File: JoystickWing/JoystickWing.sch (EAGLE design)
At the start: 19 parts, among them J1 5747844-4

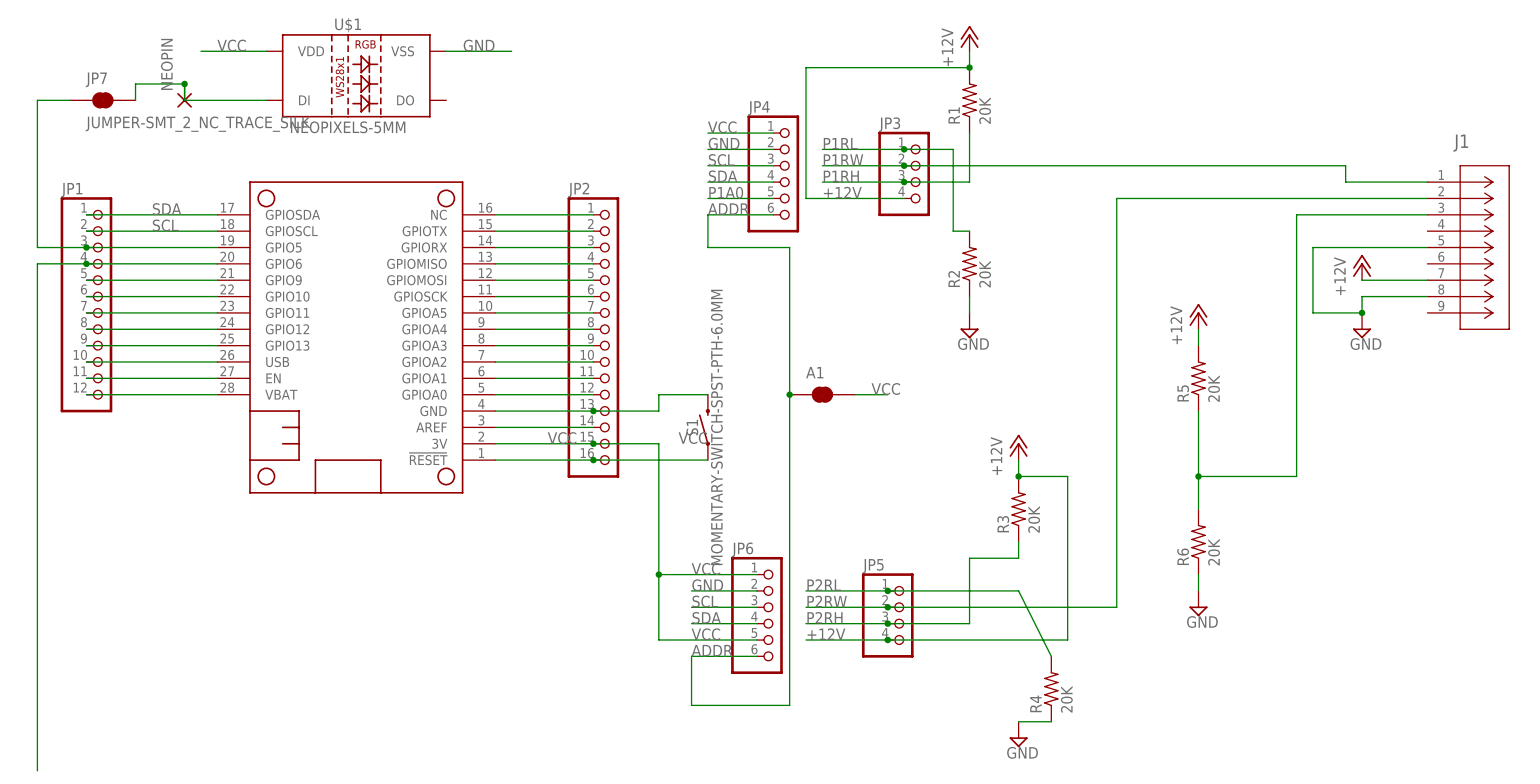
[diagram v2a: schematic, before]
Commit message: Added the missing Neopixel led pads and updated the switch to DTS-3: 3.5x6mm style switch.
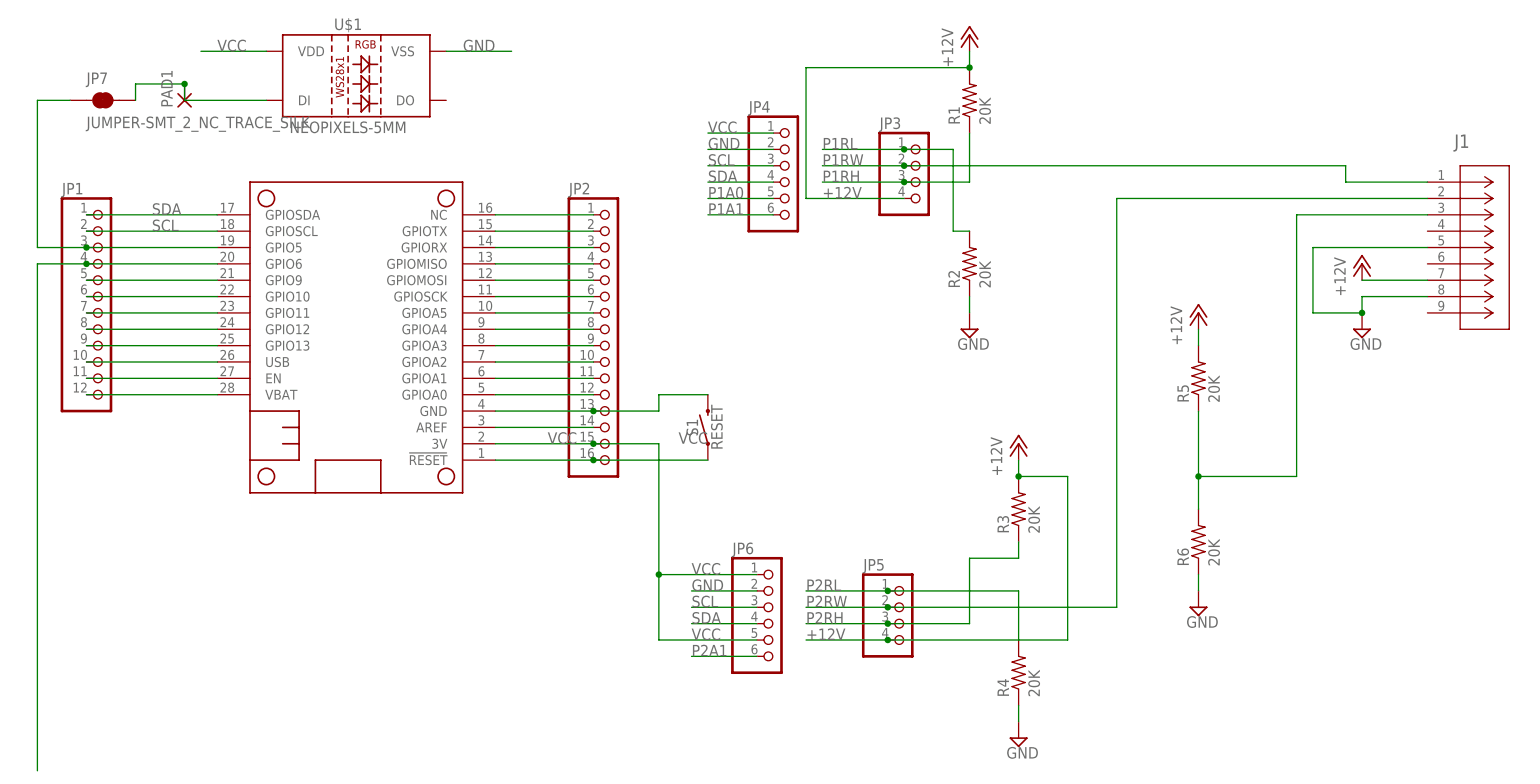
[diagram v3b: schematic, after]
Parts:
- removed A1: JUMPER-SMT_2_NC_TRACE_SILK, SparkFun-Jumpers:JUMPER-SMT_2_NC_TRACE_SILK
- S1: value MOMENTARY-SWITCH-SPST-PTH-6.0MM -> RESET; device SparkFun-Switches:MOMENTARY-SWITCH-SPST-PTH-6.0MM -> milador:SWITCH_DTS-3
- renumbered NEOPIN to PAD1
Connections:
- removed net ADDR: A1.1, JP4.6, JP6.6
- new net P1A1: JP4.6
- new net P2A1: JP6.6
- net VCC: no longer A1.2
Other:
- moved on the sheet: R4
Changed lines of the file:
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@@
 <?xml version="1.0" encoding="utf-8"?>
 <!DOCTYPE eagle SYSTEM "eagle.dtd">
-<eagle version="9.2.2">
+<eagle version="9.4.2">
 <drawing>
 <settings>
@@
 <layers>
 <layer number="1" name="Top" color="4" fill="1" visible="no" active="no"/>
+<layer number="2" name="Route2" color="1" fill="3" visible="no" active="no"/>
+<layer number="3" name="Route3" color="4" fill="3" visible="no" active="no"/>
+<layer number="4" name="Route4" color="1" fill="4" visible="no" active="no"/>
+<layer number="5" name="Route5" color="4" fill="4" visible="no" active="no"/>
+<layer number="6" name="Route6" color="1" fill="8" visible="no" active="no"/>
+<layer number="7" name="Route7" color="4" fill="8" visible="no" active="no"/>
+<layer number="8" name="Route8" color="1" fill="2" visible="no" active="no"/>
+<layer number="9" name="Route9" color="4" fill="2" visible="no" active="no"/>
+<layer number="10" name="Route10" color="1" fill="7" visible="no" active="no"/>
+<layer number="11" name="Route11" color="4" fill="7" visible="no" active="no"/>
+<layer number="12" name="Route12" color="1" fill="5" visible="no" active="no"/>
+<layer number="13" name="Route13" color="4" fill="5" visible="no" active="no"/>
+<layer number="14" name="Route14" color="1" fill="6" visible="no" active="no"/>
+<layer number="15" name="Route15" color="4" fill="6" visible="no" active="no"/>
 <layer number="16" name="Bottom" color="1" fill="1" visible="no" active="no"/>
 <layer number="17" name="Pads" color="2" fill="1" visible="no" active="no"/>
@@
 <part name="JP1" library="adafruit" library_urn="urn:adsk.eagle:library:420" deviceset="PINHD-1X12" device="-CB" package3d_urn="urn:adsk.eagle:package:6240772/1"/>
 <part name="JP2" library="pinhead" library_urn="urn:adsk.eagle:library:325" deviceset="PINHD-1X16" device="" package3d_urn="urn:adsk.eagle:package:22432/2"/>
-<part name="U$1" library="milador" deviceset="NEOPIXELS-5MM" device="" package3d_urn="urn:adsk.eagle:package:6677832/4"/>
+<part name="U$1" library="milador" library_urn="urn:adsk.eagle:library:12595918" deviceset="NEOPIXELS-5MM" device="" package3d_urn="urn:adsk.eagle:package:6677832/5"/>
 <part name="JP7" library="SparkFun-Jumpers" deviceset="JUMPER-SMT_2_NC_TRACE" device="_SILK"/>
-<part name="NEOPIN" library="wirepad" library_urn="urn:adsk.eagle:library:412" deviceset="2,54/1,1" device="" package3d_urn="urn:adsk.eagle:package:30836/1"/>
-<part name="S1" library="SparkFun-Switches" library_urn="urn:adsk.eagle:library:535" deviceset="MOMENTARY-SWITCH-SPST" device="-PTH-6.0MM" package3d_urn="urn:adsk.eagle:package:40163/1"/>
-<part name="A1" library="SparkFun-Jumpers" deviceset="JUMPER-SMT_2_NC_TRACE" device="_SILK"/>
+<part name="PAD1" library="wirepad" library_urn="urn:adsk.eagle:library:412" deviceset="2,54/1,1" device="" package3d_urn="urn:adsk.eagle:package:30836/1"/>
+<part name="S1" library="milador" library_urn="urn:adsk.eagle:library:12595918" deviceset="SWITCH_DTS-3" device="" value="RESET"/>
 </parts>
 <sheets>
@@
 <attribute name="VALUE" x="28.702" y="19.05" size="1.778" layer="96" rot="R90"/>
 </instance>
-<instance part="R4" gate="G$1" x="30.48" y="-5.08" smashed="yes" rot="R90">
-<attribute name="NAME" x="28.9814" y="-8.89" size="1.778" layer="95" rot="R90"/>
-<attribute name="VALUE" x="33.782" y="-8.89" size="1.778" layer="96" rot="R90"/>
+<instance part="R4" gate="G$1" x="25.4" y="-2.54" smashed="yes" rot="R90">
+<attribute name="NAME" x="23.9014" y="-6.35" size="1.778" layer="95" rot="R90"/>
+<attribute name="VALUE" x="28.702" y="-6.35" size="1.778" layer="96" rot="R90"/>
 </instance>
 <instance part="SUPPLY4" gate="GND" x="53.34" y="7.62" smashed="yes">
@@
 <attribute name="VALUE" x="-119.38" y="83.82" size="1.778" layer="96" font="vector" align="top-left"/>
 </instance>
-<instance part="NEOPIN" gate="1" x="-104.14" y="86.36" smashed="yes" rot="R90">
-<attribute name="NAME" x="-105.9942" y="87.757" size="1.778" layer="95" rot="R90"/>
+<instance part="PAD1" gate="1" x="-104.14" y="86.36" smashed="yes" rot="R90">
+<attribute name="NAME" x="-105.9942" y="85.217" size="1.778" layer="95" rot="R90"/>
 <attribute name="VALUE" x="-100.838" y="85.217" size="1.778" layer="96" rot="R90"/>
 </instance>
@@
 <attribute name="NAME" x="-24.384" y="35.56" size="1.778" layer="95" font="vector" rot="R90" align="bottom-center"/>
 <attribute name="VALUE" x="-22.352" y="35.56" size="1.778" layer="96" font="vector" rot="R90" align="top-center"/>
-</instance>
-<instance part="A1" gate="G$1" x="-5.08" y="40.64" smashed="yes">
-<attribute name="NAME" x="-7.62" y="43.18" size="1.778" layer="95" font="vector"/>
 </instance>
 </instances>
@@
 <pinref part="R4" gate="G$1" pin="1"/>
 <pinref part="SUPPLY3" gate="GND" pin="GND"/>
-<wire x1="30.48" y1="-10.16" x2="25.4" y2="-10.16" width="0.1524" layer="91"/>
+<wire x1="25.4" y1="-7.62" x2="25.4" y2="-10.16" width="0.1524" layer="91"/>
 </segment>
 <segment>
@@
 <label x="-99.06" y="93.98" size="1.778" layer="95"/>
 </segment>
-<segment>
-<pinref part="A1" gate="G$1" pin="2"/>
-<wire x1="0" y1="40.64" x2="5.08" y2="40.64" width="0.1524" layer="91"/>
-<label x="2.54" y="40.64" size="1.778" layer="95"/>
-</segment>
 </net>
 <net name="P1A0" class="0">
@@
 <wire x1="-12.7" y1="71.12" x2="-22.86" y2="71.12" width="0.1524" layer="91"/>
 <label x="-22.86" y="71.12" size="1.778" layer="95"/>
+</segment>
+</net>
+<net name="P1A1" class="0">
+<segment>
+<pinref part="JP4" gate="A" pin="6"/>
+<wire x1="-12.7" y1="68.58" x2="-22.86" y2="68.58" width="0.1524" layer="91"/>
+<label x="-22.86" y="68.58" size="1.778" layer="95"/>
 </segment>
 </net>
@@
 </segment>
 </net>
-<net name="ADDR" class="0">
+<net name="P2A1" class="0">
 <segment>
 <pinref part="JP6" gate="A" pin="6"/>
 <wire x1="-15.24" y1="0" x2="-25.4" y2="0" width="0.1524" layer="91"/>
 <label x="-25.4" y="0" size="1.778" layer="95"/>
-<wire x1="-25.4" y1="0" x2="-25.4" y2="-7.62" width="0.1524" layer="91"/>
-<wire x1="-25.4" y1="-7.62" x2="-10.16" y2="-7.62" width="0.1524" layer="91"/>
-<pinref part="A1" gate="G$1" pin="1"/>
-<wire x1="-10.16" y1="-7.62" x2="-10.16" y2="40.64" width="0.1524" layer="91"/>
-<wire x1="-10.16" y1="40.64" x2="-10.16" y2="63.5" width="0.1524" layer="91"/>
-<junction x="-10.16" y="40.64"/>
-<wire x1="-10.16" y1="63.5" x2="-22.86" y2="63.5" width="0.1524" layer="91"/>
-<pinref part="JP4" gate="A" pin="6"/>
-<wire x1="-12.7" y1="68.58" x2="-22.86" y2="68.58" width="0.1524" layer="91"/>
-<label x="-22.86" y="68.58" size="1.778" layer="95"/>
-<wire x1="-22.86" y1="63.5" x2="-22.86" y2="68.58" width="0.1524" layer="91"/>
 </segment>
 </net>
@@
 <pinref part="R4" gate="G$1" pin="2"/>
 <wire x1="5.08" y1="10.16" x2="25.4" y2="10.16" width="0.1524" layer="91"/>
-<wire x1="25.4" y1="10.16" x2="30.48" y2="0" width="0.1524" layer="91"/>
+<wire x1="25.4" y1="10.16" x2="25.4" y2="2.54" width="0.1524" layer="91"/>
 </segment>
 </net>
@@
 <segment>
 <pinref part="U$1" gate="G$1" pin="DI"/>
-<pinref part="NEOPIN" gate="1" pin="P"/>
+<pinref part="PAD1" gate="1" pin="P"/>
 <wire x1="-91.44" y1="86.36" x2="-104.14" y2="86.36" width="0.1524" layer="91"/>
 <wire x1="-104.14" y1="86.36" x2="-104.14" y2="88.9" width="0.1524" layer="91"/>

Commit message: Revert "Added the missing Neopixel led pads and updated the switch to DTS-3: 3.5x6mm style switch."
This reverts commit 7139ee0b9ca13871835c94f32c5504dad1631a27.
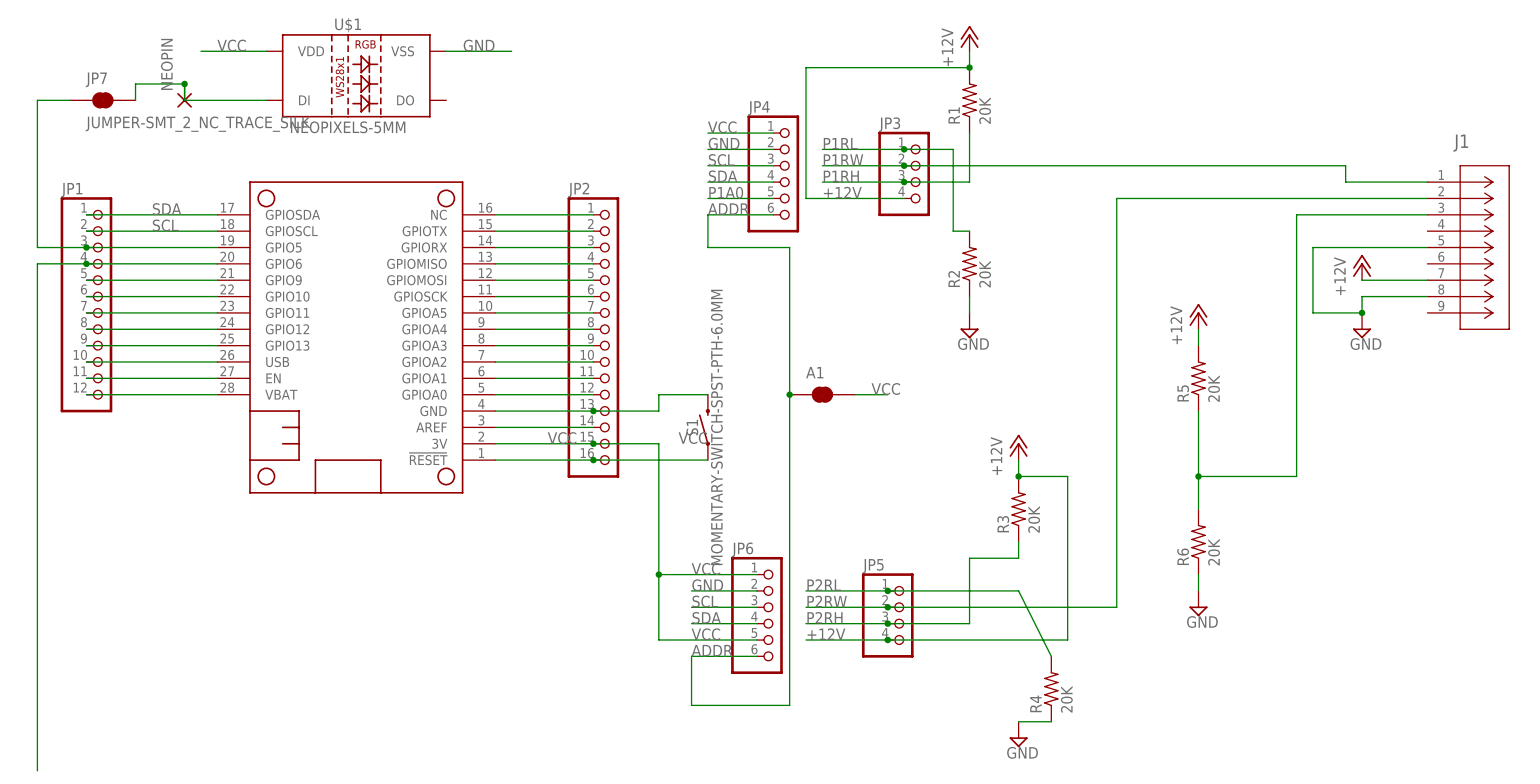
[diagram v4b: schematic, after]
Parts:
- added A1: JUMPER-SMT_2_NC_TRACE_SILK, SparkFun-Jumpers:JUMPER-SMT_2_NC_TRACE_SILK
- S1: value RESET -> MOMENTARY-SWITCH-SPST-PTH-6.0MM; device milador:SWITCH_DTS-3 -> SparkFun-Switches:MOMENTARY-SWITCH-SPST-PTH-6.0MM
- renumbered PAD1 to NEOPIN
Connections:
- removed net P1A1: JP4.6
- removed net P2A1: JP6.6
- new net ADDR: A1.1, JP4.6, JP6.6
- net VCC: now also A1.2
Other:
- moved on the sheet: R4
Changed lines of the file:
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@@
 <?xml version="1.0" encoding="utf-8"?>
 <!DOCTYPE eagle SYSTEM "eagle.dtd">
-<eagle version="9.4.2">
+<eagle version="9.2.2">
 <drawing>
 <settings>
@@
 <layers>
 <layer number="1" name="Top" color="4" fill="1" visible="no" active="no"/>
-<layer number="2" name="Route2" color="1" fill="3" visible="no" active="no"/>
-<layer number="3" name="Route3" color="4" fill="3" visible="no" active="no"/>
-<layer number="4" name="Route4" color="1" fill="4" visible="no" active="no"/>
-<layer number="5" name="Route5" color="4" fill="4" visible="no" active="no"/>
-<layer number="6" name="Route6" color="1" fill="8" visible="no" active="no"/>
-<layer number="7" name="Route7" color="4" fill="8" visible="no" active="no"/>
-<layer number="8" name="Route8" color="1" fill="2" visible="no" active="no"/>
-<layer number="9" name="Route9" color="4" fill="2" visible="no" active="no"/>
-<layer number="10" name="Route10" color="1" fill="7" visible="no" active="no"/>
-<layer number="11" name="Route11" color="4" fill="7" visible="no" active="no"/>
-<layer number="12" name="Route12" color="1" fill="5" visible="no" active="no"/>
-<layer number="13" name="Route13" color="4" fill="5" visible="no" active="no"/>
-<layer number="14" name="Route14" color="1" fill="6" visible="no" active="no"/>
-<layer number="15" name="Route15" color="4" fill="6" visible="no" active="no"/>
 <layer number="16" name="Bottom" color="1" fill="1" visible="no" active="no"/>
 <layer number="17" name="Pads" color="2" fill="1" visible="no" active="no"/>
@@
 <part name="JP1" library="adafruit" library_urn="urn:adsk.eagle:library:420" deviceset="PINHD-1X12" device="-CB" package3d_urn="urn:adsk.eagle:package:6240772/1"/>
 <part name="JP2" library="pinhead" library_urn="urn:adsk.eagle:library:325" deviceset="PINHD-1X16" device="" package3d_urn="urn:adsk.eagle:package:22432/2"/>
-<part name="U$1" library="milador" library_urn="urn:adsk.eagle:library:12595918" deviceset="NEOPIXELS-5MM" device="" package3d_urn="urn:adsk.eagle:package:6677832/5"/>
+<part name="U$1" library="milador" deviceset="NEOPIXELS-5MM" device="" package3d_urn="urn:adsk.eagle:package:6677832/4"/>
 <part name="JP7" library="SparkFun-Jumpers" deviceset="JUMPER-SMT_2_NC_TRACE" device="_SILK"/>
-<part name="PAD1" library="wirepad" library_urn="urn:adsk.eagle:library:412" deviceset="2,54/1,1" device="" package3d_urn="urn:adsk.eagle:package:30836/1"/>
-<part name="S1" library="milador" library_urn="urn:adsk.eagle:library:12595918" deviceset="SWITCH_DTS-3" device="" value="RESET"/>
+<part name="NEOPIN" library="wirepad" library_urn="urn:adsk.eagle:library:412" deviceset="2,54/1,1" device="" package3d_urn="urn:adsk.eagle:package:30836/1"/>
+<part name="S1" library="SparkFun-Switches" library_urn="urn:adsk.eagle:library:535" deviceset="MOMENTARY-SWITCH-SPST" device="-PTH-6.0MM" package3d_urn="urn:adsk.eagle:package:40163/1"/>
+<part name="A1" library="SparkFun-Jumpers" deviceset="JUMPER-SMT_2_NC_TRACE" device="_SILK"/>
 </parts>
 <sheets>
@@
 <attribute name="VALUE" x="28.702" y="19.05" size="1.778" layer="96" rot="R90"/>
 </instance>
-<instance part="R4" gate="G$1" x="25.4" y="-2.54" smashed="yes" rot="R90">
-<attribute name="NAME" x="23.9014" y="-6.35" size="1.778" layer="95" rot="R90"/>
-<attribute name="VALUE" x="28.702" y="-6.35" size="1.778" layer="96" rot="R90"/>
+<instance part="R4" gate="G$1" x="30.48" y="-5.08" smashed="yes" rot="R90">
+<attribute name="NAME" x="28.9814" y="-8.89" size="1.778" layer="95" rot="R90"/>
+<attribute name="VALUE" x="33.782" y="-8.89" size="1.778" layer="96" rot="R90"/>
 </instance>
 <instance part="SUPPLY4" gate="GND" x="53.34" y="7.62" smashed="yes">
@@
 <attribute name="VALUE" x="-119.38" y="83.82" size="1.778" layer="96" font="vector" align="top-left"/>
 </instance>
-<instance part="PAD1" gate="1" x="-104.14" y="86.36" smashed="yes" rot="R90">
-<attribute name="NAME" x="-105.9942" y="85.217" size="1.778" layer="95" rot="R90"/>
+<instance part="NEOPIN" gate="1" x="-104.14" y="86.36" smashed="yes" rot="R90">
+<attribute name="NAME" x="-105.9942" y="87.757" size="1.778" layer="95" rot="R90"/>
 <attribute name="VALUE" x="-100.838" y="85.217" size="1.778" layer="96" rot="R90"/>
 </instance>
@@
 <attribute name="NAME" x="-24.384" y="35.56" size="1.778" layer="95" font="vector" rot="R90" align="bottom-center"/>
 <attribute name="VALUE" x="-22.352" y="35.56" size="1.778" layer="96" font="vector" rot="R90" align="top-center"/>
+</instance>
+<instance part="A1" gate="G$1" x="-5.08" y="40.64" smashed="yes">
+<attribute name="NAME" x="-7.62" y="43.18" size="1.778" layer="95" font="vector"/>
 </instance>
 </instances>
@@
 <pinref part="R4" gate="G$1" pin="1"/>
 <pinref part="SUPPLY3" gate="GND" pin="GND"/>
-<wire x1="25.4" y1="-7.62" x2="25.4" y2="-10.16" width="0.1524" layer="91"/>
+<wire x1="30.48" y1="-10.16" x2="25.4" y2="-10.16" width="0.1524" layer="91"/>
 </segment>
 <segment>
@@
 <label x="-99.06" y="93.98" size="1.778" layer="95"/>
 </segment>
+<segment>
+<pinref part="A1" gate="G$1" pin="2"/>
+<wire x1="0" y1="40.64" x2="5.08" y2="40.64" width="0.1524" layer="91"/>
+<label x="2.54" y="40.64" size="1.778" layer="95"/>
+</segment>
 </net>
 <net name="P1A0" class="0">
@@
 <wire x1="-12.7" y1="71.12" x2="-22.86" y2="71.12" width="0.1524" layer="91"/>
 <label x="-22.86" y="71.12" size="1.778" layer="95"/>
-</segment>
-</net>
-<net name="P1A1" class="0">
-<segment>
-<pinref part="JP4" gate="A" pin="6"/>
-<wire x1="-12.7" y1="68.58" x2="-22.86" y2="68.58" width="0.1524" layer="91"/>
-<label x="-22.86" y="68.58" size="1.778" layer="95"/>
 </segment>
 </net>
@@
 </segment>
 </net>
-<net name="P2A1" class="0">
+<net name="ADDR" class="0">
 <segment>
 <pinref part="JP6" gate="A" pin="6"/>
 <wire x1="-15.24" y1="0" x2="-25.4" y2="0" width="0.1524" layer="91"/>
 <label x="-25.4" y="0" size="1.778" layer="95"/>
+<wire x1="-25.4" y1="0" x2="-25.4" y2="-7.62" width="0.1524" layer="91"/>
+<wire x1="-25.4" y1="-7.62" x2="-10.16" y2="-7.62" width="0.1524" layer="91"/>
+<pinref part="A1" gate="G$1" pin="1"/>
+<wire x1="-10.16" y1="-7.62" x2="-10.16" y2="40.64" width="0.1524" layer="91"/>
+<wire x1="-10.16" y1="40.64" x2="-10.16" y2="63.5" width="0.1524" layer="91"/>
+<junction x="-10.16" y="40.64"/>
+<wire x1="-10.16" y1="63.5" x2="-22.86" y2="63.5" width="0.1524" layer="91"/>
+<pinref part="JP4" gate="A" pin="6"/>
+<wire x1="-12.7" y1="68.58" x2="-22.86" y2="68.58" width="0.1524" layer="91"/>
+<label x="-22.86" y="68.58" size="1.778" layer="95"/>
+<wire x1="-22.86" y1="63.5" x2="-22.86" y2="68.58" width="0.1524" layer="91"/>
 </segment>
 </net>
@@
 <pinref part="R4" gate="G$1" pin="2"/>
 <wire x1="5.08" y1="10.16" x2="25.4" y2="10.16" width="0.1524" layer="91"/>
-<wire x1="25.4" y1="10.16" x2="25.4" y2="2.54" width="0.1524" layer="91"/>
+<wire x1="25.4" y1="10.16" x2="30.48" y2="0" width="0.1524" layer="91"/>
 </segment>
 </net>
@@
 <segment>
 <pinref part="U$1" gate="G$1" pin="DI"/>
-<pinref part="PAD1" gate="1" pin="P"/>
+<pinref part="NEOPIN" gate="1" pin="P"/>
 <wire x1="-91.44" y1="86.36" x2="-104.14" y2="86.36" width="0.1524" layer="91"/>
 <wire x1="-104.14" y1="86.36" x2="-104.14" y2="88.9" width="0.1524" layer="91"/>
